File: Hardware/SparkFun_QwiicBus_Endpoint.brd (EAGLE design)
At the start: 44.5 x 25.4 mm, 66 parts, among them J1 QWIIC_RIGHT_ANGLE, J2 QWIIC_RIGHT_ANGLE, J3 RJ45, U1 PCA9615

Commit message: post design review and checklist changes
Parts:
- removed J6: (no value), SparkX:1X04_NO_SILK
- added J8: (no value), SparkFun-Connectors:1X04_NO_SILK
- added LOGO3: QWIIC_LOGO_4MM, SparkFun-Aesthetics:QWIIC_4MM
- J1, J2: value QWIIC_RIGHT_ANGLE -> QWIIC
- moved LOGO2 31.8 mm to (-5.08, -11.4)
- moved FD1 5.39 mm to (1.27, 5.08)
- moved FD3 5.39 mm to (1.27, 5.08)
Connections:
- net GND: now also J8.1; no longer J6.1
- net SCL: now also J8.4; no longer J6.4
- net SDA: now also J8.3; no longer J6.3
- net VDD_A: now also J8.2; no longer J6.2
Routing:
- net GRN_P: track 15.5 -> 14.7 mm
- net SCL: track 43.2 -> 43.7 mm
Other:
- board text added: "Andy England"
- board text removed: "Measurements in mm"

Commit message: qc double check changes
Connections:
- net DSCL+ renamed DSCL_P
- net DSCL- renamed DSCL_N
- net DSDA+ renamed DSDA_P
- net DSDA- renamed DSDA_N
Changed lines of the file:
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@@
 <vertex x="44.45" y="25.4"/>
 </polygon>
-<wire x1="16.51" y1="11.7094" x2="16.5131" y2="11.7125" width="0.254" layer="1"/>
-<wire x1="16.5131" y1="11.7125" x2="16.791" y2="11.7125" width="0.254" layer="1"/>
 <contactref element="GND" pad="1"/>
 <contactref element="J4" pad="1"/>
@@
 <via x="12.2" y="6.604" extent="1-16" drill="0.381"/>
 <wire x1="18.5293" y1="17.145" x2="18.5293" y2="17.3863" width="0.254" layer="1"/>
-<wire x1="18.5293" y1="17.3863" x2="18.542" y2="17.399" width="0.254" layer="1"/>
 <contactref element="J8" pad="2"/>
 <wire x1="3.81" y1="15.24" x2="1.27" y2="15.24" width="0.254" layer="1"/>
@@
 <wire x1="26.035" y1="15.621" x2="24.511" y2="17.145" width="0.254" layer="16"/>
 <wire x1="19.5707" y1="17.145" x2="19.5707" y2="17.3863" width="0.254" layer="1"/>
-<wire x1="19.5707" y1="17.3863" x2="19.558" y2="17.399" width="0.254" layer="1"/>
 </signal>
 <signal name="EN">
@@
 <wire x1="14.097" y1="9.017" x2="14.097" y2="12.319" width="0.254" layer="16"/>
 </signal>
-<signal name="DSDA-">
+<signal name="DSDA_N">
 <contactref element="U1" pad="9"/>
 <contactref element="R5" pad="1"/>
@@
 <wire x1="30.353" y1="18.542" x2="30.988" y2="19.177" width="0.254" layer="1"/>
 </signal>
-<signal name="DSDA+">
+<signal name="DSDA_P">
 <contactref element="U1" pad="8"/>
 <contactref element="R4" pad="1"/>
@@
 <wire x1="30.861" y1="18.288" x2="31.242" y2="18.669" width="0.254" layer="1"/>
 </signal>
-<signal name="DSCL+">
+<signal name="DSCL_P">
 <contactref element="U1" pad="7"/>
 <contactref element="R1" pad="1"/>
@@
 <wire x1="24.1045" y1="12.2175" x2="25.019" y2="11.303" width="0.254" layer="1"/>
 <wire x1="27.79" y1="10.795" x2="27.79" y2="9.779" width="0.254" layer="1"/>
-<wire x1="32.385" y1="7.874" x2="33.528" y2="9.017" width="0.254" layer="1"/>
-<wire x1="33.528" y1="9.017" x2="33.528" y2="9.271" width="0.254" layer="1"/>
+<wire x1="32.512" y1="7.874" x2="33.528" y2="8.89" width="0.254" layer="1"/>
+<wire x1="33.528" y1="8.89" x2="33.528" y2="9.271" width="0.254" layer="1"/>
 <wire x1="33.528" y1="9.271" x2="33.274" y2="9.525" width="0.254" layer="1"/>
 <wire x1="33.274" y1="9.525" x2="32.385" y2="9.525" width="0.254" layer="1"/>
@@
 <wire x1="30.734" y1="9.906" x2="30.734" y2="8.382" width="0.254" layer="1"/>
 <wire x1="30.734" y1="8.382" x2="31.242" y2="7.874" width="0.254" layer="1"/>
-<wire x1="31.242" y1="7.874" x2="32.385" y2="7.874" width="0.254" layer="1"/>
-</signal>
-<signal name="DSCL-">
+<wire x1="31.242" y1="7.874" x2="32.512" y2="7.874" width="0.254" layer="1"/>
+</signal>
+<signal name="DSCL_N">
 <contactref element="U1" pad="6"/>
 <contactref element="R2" pad="1"/>
@@
 <contactref element="J3" pad="3"/>
 <contactref element="J7" pad="2"/>
-<wire x1="29.21" y1="1.27" x2="29.355615625" y2="1.415615625" width="0.3048" layer="16"/>
 <wire x1="33.655" y1="8.9989375" x2="32.9110625" y2="8.255" width="0.3048" layer="16"/>
 <wire x1="33.655" y1="9.525" x2="33.655" y2="8.9989375" width="0.3048" layer="16"/>
@@
 <contactref element="J3" pad="6"/>
 <contactref element="J7" pad="1"/>
-<wire x1="26.67" y1="1.27" x2="26.714015625" y2="1.314015625" width="0.3048" layer="16"/>
 <wire x1="32.9110625" y1="10.795" x2="31.665978125" y2="10.795" width="0.3048" layer="16"/>
 <wire x1="33.655" y1="11.5389375" x2="32.9110625" y2="10.795" width="0.3048" layer="16"/>

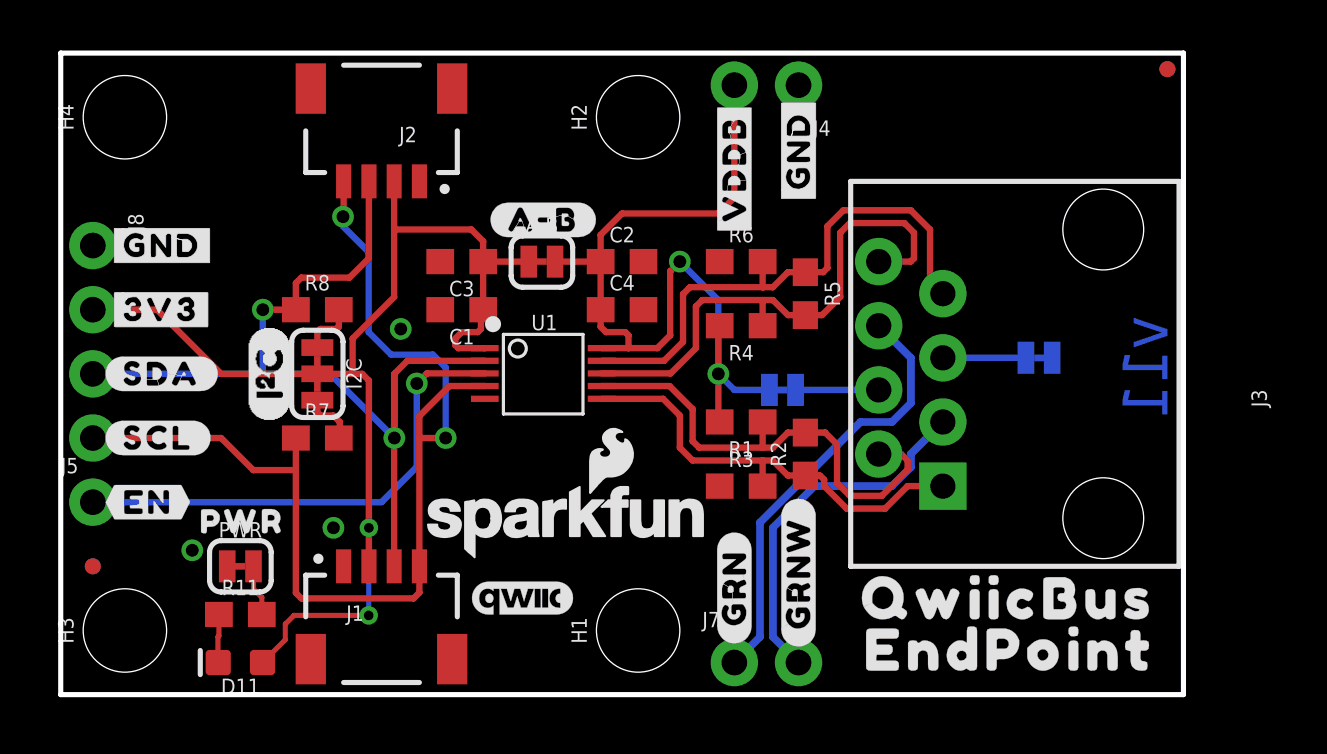
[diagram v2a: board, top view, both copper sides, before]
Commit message: adding qwiicBus silk
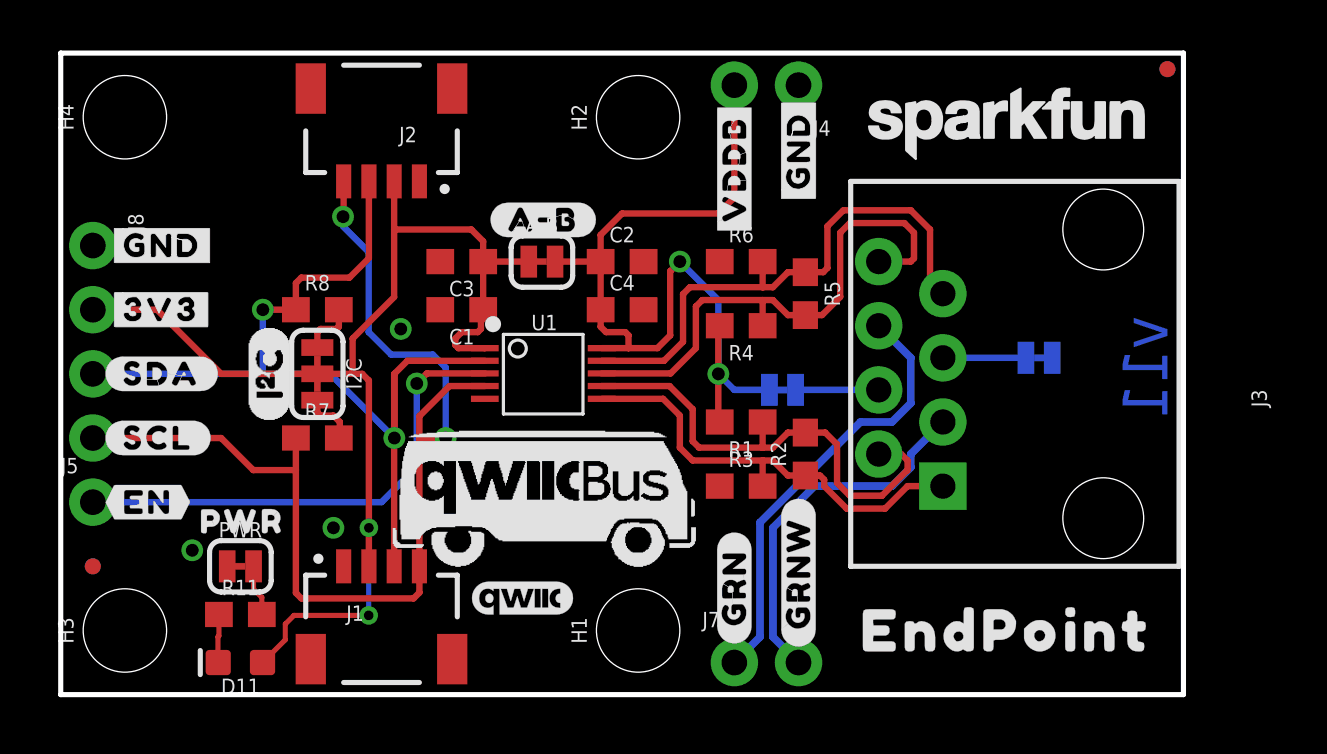
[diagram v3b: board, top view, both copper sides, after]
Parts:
- removed U$24: (no value), output:QWIICBUS0
- added LOGO4: SFE_LOGO_NAME_FLAME.1_INCH, SparkFun-Aesthetics:SFE_LOGO_NAME_FLAME_.1
- added U$28: (no value), QwiicBus#working#Logo#jpg (2):QWIICBUS#WORKING#LOGO#JPG
- LOGO5: value SFE_LOGO_NAME_FLAME.1_INCH -> SFE_LOGO_NAME.1_INCH; device SparkFun-Aesthetics:SFE_LOGO_NAME_FLAME_.1 -> SparkFun-Aesthetics:SFE_LOGO_NAME_.1
- U$23: device output:QWIICBUS0 -> QwiicBus#working#Logo#jpg (2):QWIICBUS#WORKING#LOGO#JPG
- moved LOGO5 23.5 mm to (37.5, 22.6)
- moved U$26 20.0 mm to (25.8, 9.53)
- moved U$23 15.7 mm to (18.4, 13.9), flipped to the bottom
- moved LOGO1 7.98 mm to (12.7, 2.54)
- moved U$25 0.77 mm to (30.5, 2.54)
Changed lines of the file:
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@@
 <attribute name="VALUE" x="30.48" y="26.162" size="0.6096" layer="27" font="vector" ratio="20" rot="R180"/>
 </element>
-<element name="LOGO1" library="SparkFun-Aesthetics" package="OSHW-LOGO-M" value="OSHW-LOGOM" x="19.05" y="7.366" smashed="yes" rot="MR0"/>
+<element name="LOGO1" library="SparkFun-Aesthetics" package="OSHW-LOGO-M" value="OSHW-LOGOM" x="12.7" y="2.54" smashed="yes" rot="MR0"/>
 <element name="VDDB" library="SparkFun-Jumpers" package="SMT-JUMPER_2_NC_TRACE_SILK" package3d_urn="urn:adsk.eagle:package:39281/1" value="JUMPER-SMT_2_NC_TRACE_SILK" x="28.575" y="12.065" smashed="yes" rot="MR180">
 <attribute name="NAME" x="28.575" y="10.922" size="0.6096" layer="26" font="vector" ratio="20" rot="MR180" align="bottom-center"/>
@@
 <element name="FD3" library="SparkFun-Aesthetics" package="FIDUCIAL-MICRO" value="FIDUCIALUFIDUCIAL" x="1.27" y="5.08" smashed="yes" rot="MR0"/>
 <element name="FD4" library="SparkFun-Aesthetics" package="FIDUCIAL-MICRO" value="FIDUCIALUFIDUCIAL" x="43.815" y="24.765" smashed="yes" rot="MR0"/>
-<element name="LOGO5" library="SparkFun-Aesthetics" package="SFE_LOGO_NAME_FLAME_.1" value="SFE_LOGO_NAME_FLAME.1_INCH" x="20.066" y="6.858" smashed="yes"/>
+<element name="LOGO5" library="SparkFun-Aesthetics" package="SFE_LOGO_NAME_.1" value="SFE_LOGO_NAME.1_INCH" x="37.465" y="22.606" smashed="yes"/>
 <element name="J5" library="SparkFun-Connectors" package="1X01_NO_SILK" value="" x="1.27" y="7.62" smashed="yes">
 <attribute name="NAME" x="0" y="8.763" size="0.6096" layer="25" font="vector" ratio="20"/>
@@
 <element name="U$21" library="output" package="#GRN#0" value="" x="26.67" y="2.032" smashed="yes" rot="R90"/>
 <element name="U$22" library="output" package="#GRN#0" value="" x="26.67" y="6.35" smashed="yes" rot="MR270"/>
-<element name="U$23" library="output" package="QWIICBUS0" value="" x="30.48" y="3.81" smashed="yes"/>
-<element name="U$24" library="output" package="QWIICBUS0" value="" x="44.45" y="3.81" smashed="yes" rot="MR0"/>
-<element name="U$25" library="output" package="ENDPOINT0" value="" x="30.607" y="1.778" smashed="yes"/>
-<element name="U$26" library="output" package="ENDPOINT0" value="" x="44.196" y="1.778" smashed="yes" rot="MR0"/>
+<element name="U$25" library="output" package="ENDPOINT0" value="" x="30.48" y="2.54" smashed="yes"/>
+<element name="U$26" library="output" package="ENDPOINT0" value="" x="25.781" y="9.525" smashed="yes" rot="MR0"/>
 <element name="R11" library="SparkFun-Resistors" package="0603" value="1k" x="7.112" y="3.175" smashed="yes">
 <attribute name="NAME" x="7.112" y="3.937" size="0.6096" layer="25" font="vector" ratio="20" align="bottom-center"/>
@@
 </element>
 <element name="LOGO3" library="SparkFun-Aesthetics" package="QWIIC_4MM" value="QWIIC_LOGO_4MM" x="18.288" y="3.81" smashed="yes"/>
+<element name="LOGO4" library="SparkFun-Aesthetics" package="SFE_LOGO_NAME_FLAME_.1" value="SFE_LOGO_NAME_FLAME.1_INCH" x="19.05" y="17.78" smashed="yes" rot="MR0"/>
+<element name="U$28" library="QwiicBus#working#Logo#jpg (2)" package="QWIICBUS#WORKING#LOGO#JPG" value="" x="19.558" y="8.128" smashed="yes"/>
+<element name="U$23" library="QwiicBus#working#Logo#jpg (2)" package="QWIICBUS#WORKING#LOGO#JPG" value="" x="18.442" y="13.874" smashed="yes" rot="MR0"/>
 </elements>
 <signals>

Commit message: moving qwiicBus up a tad
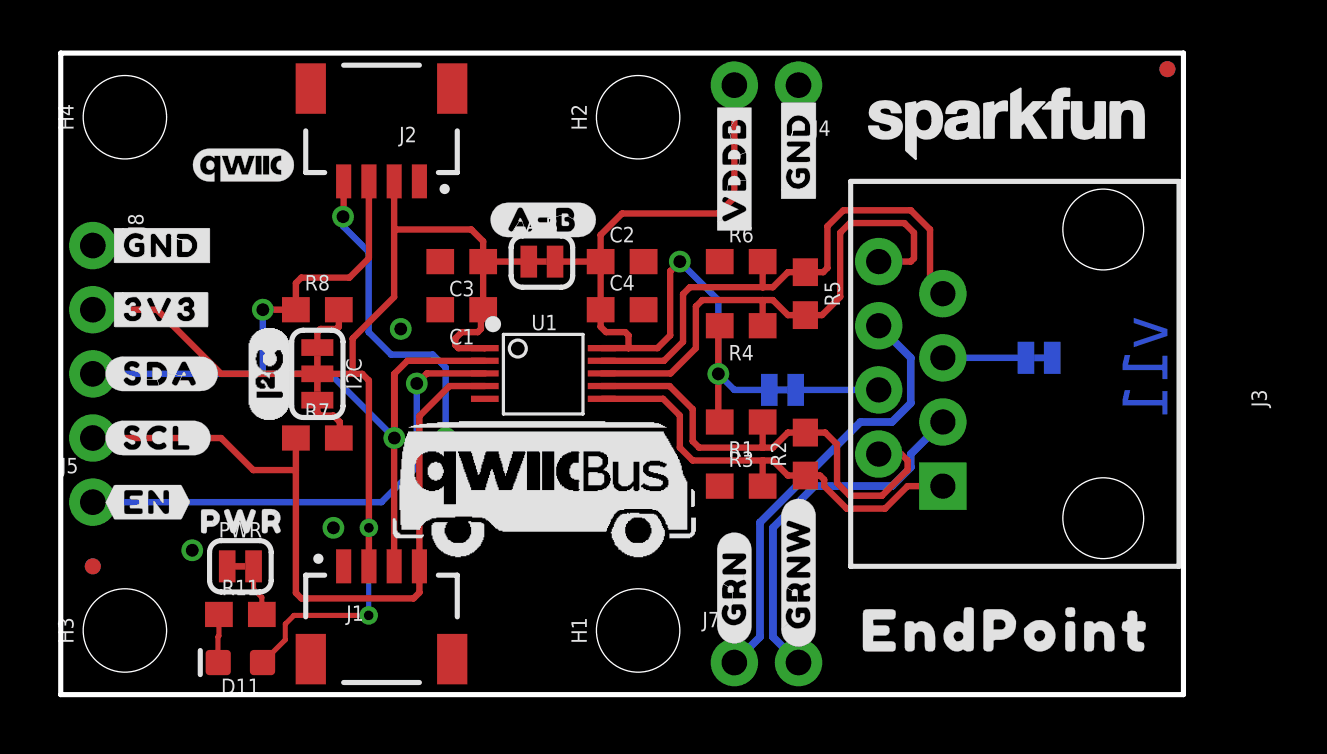
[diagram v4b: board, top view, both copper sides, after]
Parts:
- moved LOGO3 20.4 mm to (7.24, 21.0)
- moved U$28 0.38 mm to (19.6, 8.51)

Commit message: thickening VDDB trace
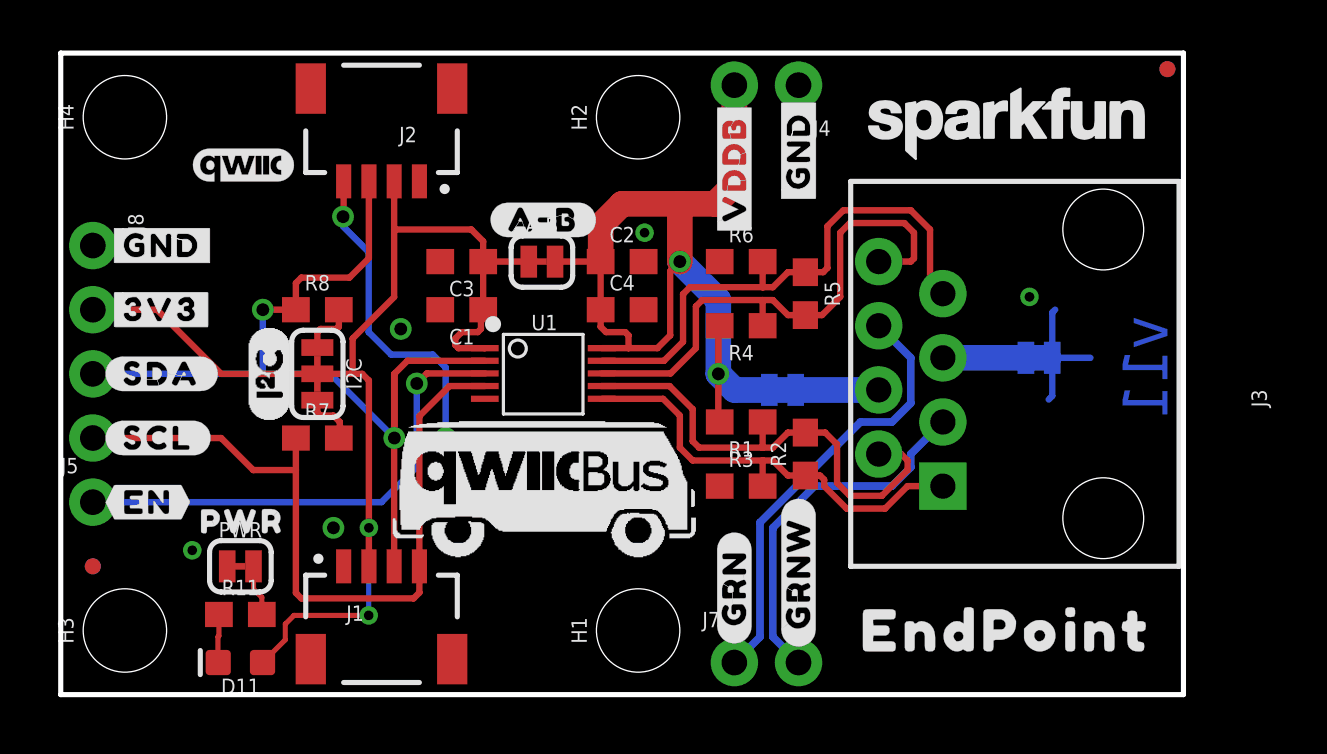
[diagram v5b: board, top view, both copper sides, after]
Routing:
- net GND: track 0.00 -> 5.17 mm, vias 3 -> 5
- net VDD_B: track 35.1 -> 37.3 mm
- net N$1: track 3.29 -> 4.32 mm
- net N$2: track 3.29 -> 4.19 mm
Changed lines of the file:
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@@
 <contactref element="J4" pad="1"/>
 <via x="10.795" y="6.604" extent="1-16" drill="0.508"/>
-<via x="5.207" y="5.715" extent="1-16" drill="0.508"/>
+<via x="5.207" y="5.715" extent="1-16" drill="0.381"/>
 <via x="13.462" y="14.478" extent="1-16" drill="0.508"/>
 <contactref element="PWR" pad="1"/>
 <contactref element="J8" pad="1"/>
+<via x="23.114" y="18.288" extent="1-16" drill="0.381"/>
+<via x="38.354" y="15.748" extent="1-16" drill="0.381"/>
+<wire x1="39.2557" y1="13.335" x2="39.2557" y2="15.1257" width="0.254" layer="16"/>
+<wire x1="39.2557" y1="15.1257" x2="39.37" y2="15.24" width="0.254" layer="16"/>
+<wire x1="39.2557" y1="13.335" x2="40.767" y2="13.335" width="0.254" layer="16"/>
+<wire x1="39.2557" y1="13.335" x2="39.2557" y2="11.8237" width="0.254" layer="16"/>
+<wire x1="39.2557" y1="11.8237" x2="39.116" y2="11.684" width="0.254" layer="16"/>
 </signal>
 <signal name="VDD_A">
@@
 <wire x1="26.09" y1="14.605" x2="26.035" y2="14.55" width="0.254" layer="1"/>
 <wire x1="26.035" y1="14.55" x2="26.035" y2="12.7" width="0.254" layer="1"/>
-<wire x1="28.0543" y1="12.065" x2="26.67" y2="12.065" width="0.254" layer="16"/>
-<wire x1="26.67" y1="12.065" x2="26.035" y2="12.7" width="0.254" layer="16"/>
-<wire x1="26.035" y1="15.621" x2="26.035" y2="12.7" width="0.254" layer="16"/>
-<wire x1="22.225" y1="19.05" x2="21.375" y2="18.2" width="0.254" layer="1"/>
-<wire x1="21.375" y1="18.2" x2="21.375" y2="17.145" width="0.254" layer="1"/>
-<wire x1="22.225" y1="19.05" x2="26.035" y2="19.05" width="0.254" layer="1"/>
-<wire x1="26.035" y1="19.05" x2="26.67" y2="19.685" width="0.254" layer="1"/>
-<wire x1="26.67" y1="19.685" x2="26.67" y2="24.13" width="0.254" layer="1"/>
+<wire x1="28.0543" y1="12.065" x2="26.67" y2="12.065" width="1.016" layer="16"/>
+<wire x1="26.67" y1="12.065" x2="26.035" y2="12.7" width="1.016" layer="16"/>
+<wire x1="26.035" y1="15.621" x2="26.035" y2="12.7" width="1.016" layer="16"/>
+<wire x1="22.225" y1="19.431" x2="21.375" y2="18.581" width="1.016" layer="1"/>
+<wire x1="21.375" y1="18.581" x2="21.375" y2="17.145" width="1.016" layer="1"/>
+<wire x1="22.225" y1="19.431" x2="24.511" y2="19.431" width="1.016" layer="1"/>
+<wire x1="24.511" y1="19.431" x2="25.908" y2="19.431" width="1.016" layer="1"/>
+<wire x1="25.908" y1="19.431" x2="26.67" y2="20.193" width="1.016" layer="1"/>
+<wire x1="26.67" y1="20.193" x2="26.67" y2="24.13" width="1.016" layer="1"/>
 <wire x1="24.13" y1="14.224" x2="24.13" y2="16.764" width="0.254" layer="1"/>
 <wire x1="24.13" y1="16.764" x2="24.511" y2="17.145" width="0.254" layer="1"/>
-<wire x1="26.035" y1="15.621" x2="24.511" y2="17.145" width="0.254" layer="16"/>
+<wire x1="26.035" y1="15.621" x2="24.511" y2="17.145" width="1.016" layer="16"/>
 <wire x1="19.5707" y1="17.145" x2="19.5707" y2="17.3863" width="0.254" layer="1"/>
+<wire x1="24.511" y1="17.145" x2="24.511" y2="19.431" width="1.016" layer="1"/>
 </signal>
 <signal name="EN">
@@
 <contactref element="VDDB" pad="2"/>
 <contactref element="J3" pad="4"/>
-<wire x1="29.0957" y1="12.065" x2="32.385" y2="12.065" width="0.254" layer="16"/>
+<wire x1="29.0957" y1="12.065" x2="32.385" y2="12.065" width="1.016" layer="16"/>
+<wire x1="29.0957" y1="12.065" x2="28.067" y2="12.065" width="1.016" layer="16"/>
 </signal>
 <signal name="N$2">
 <contactref element="GND" pad="2"/>
 <contactref element="J3" pad="5"/>
-<wire x1="38.2143" y1="13.335" x2="34.925" y2="13.335" width="0.254" layer="16"/>
+<wire x1="38.2143" y1="13.335" x2="34.925" y2="13.335" width="1.016" layer="16"/>
+<wire x1="38.2143" y1="13.335" x2="39.116" y2="13.335" width="1.016" layer="16"/>
 </signal>
 <signal name="GRN_P">
